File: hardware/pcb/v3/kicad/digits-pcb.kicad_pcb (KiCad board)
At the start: 2 copper layers, 61.9 x 76.2 mm, 77 parts, among them J8 Conn_01x04, SW1 Hook_DPDT, SW2 SW_Push, U10 XL6019E1, U2 DRV8871DDAR, U3 RP2040, U4 W25Q16JVSSIQ, U5 AMS1117-3.3, U6 TLV320AIC3104IRHBR, U7 XC6206P182MR, Y1 ABM8-272-T3

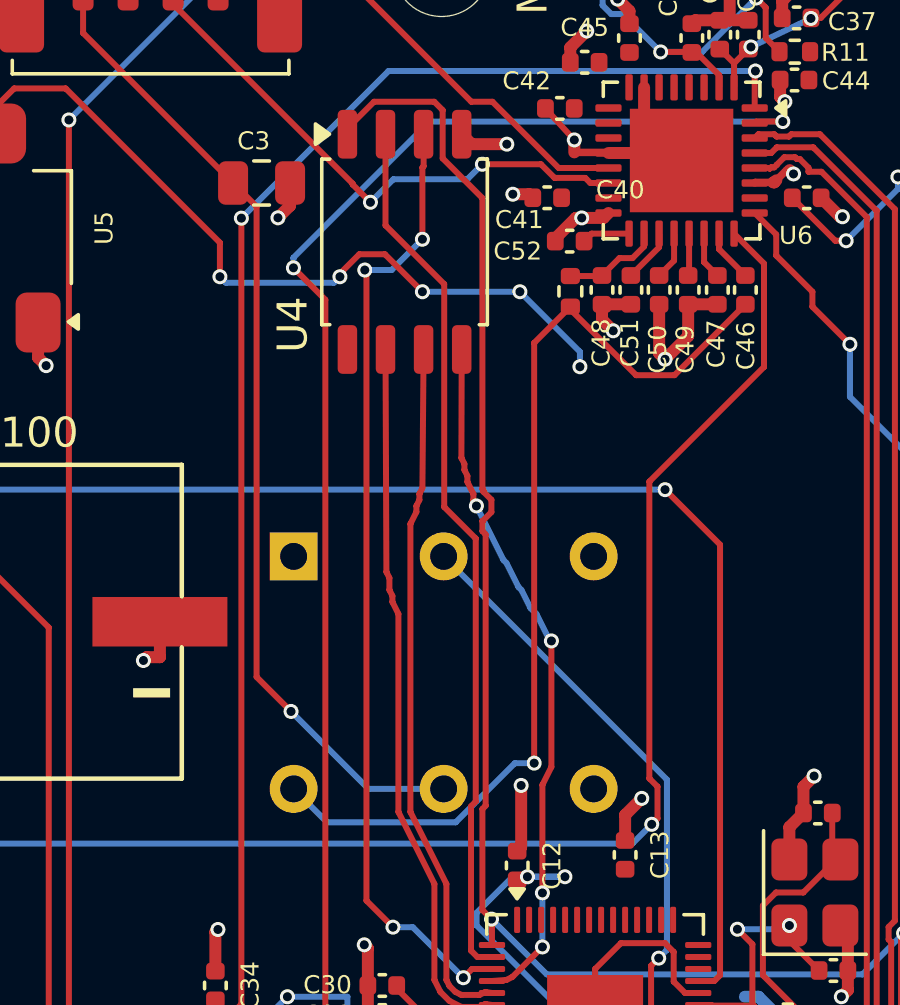
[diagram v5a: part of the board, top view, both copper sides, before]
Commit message: fix(hardware): route SW1 corrected DPDT pin mapping on the PCB
Update-PCB-from-Schematic for the SW1 re-pin (e2b5f92, 6b79142): HOOK_SW,
MIC_FROM_SW, and MIC_HOT moved to pads 3, 4, 6 and rerouted; pad 2 GND
unchanged. BOM regenerated via the JLCPCB toolkit (SW2 now carries C87036,
connector refs annotated). DRC clean: 0 errors, 0 unconnected, 0 parity.
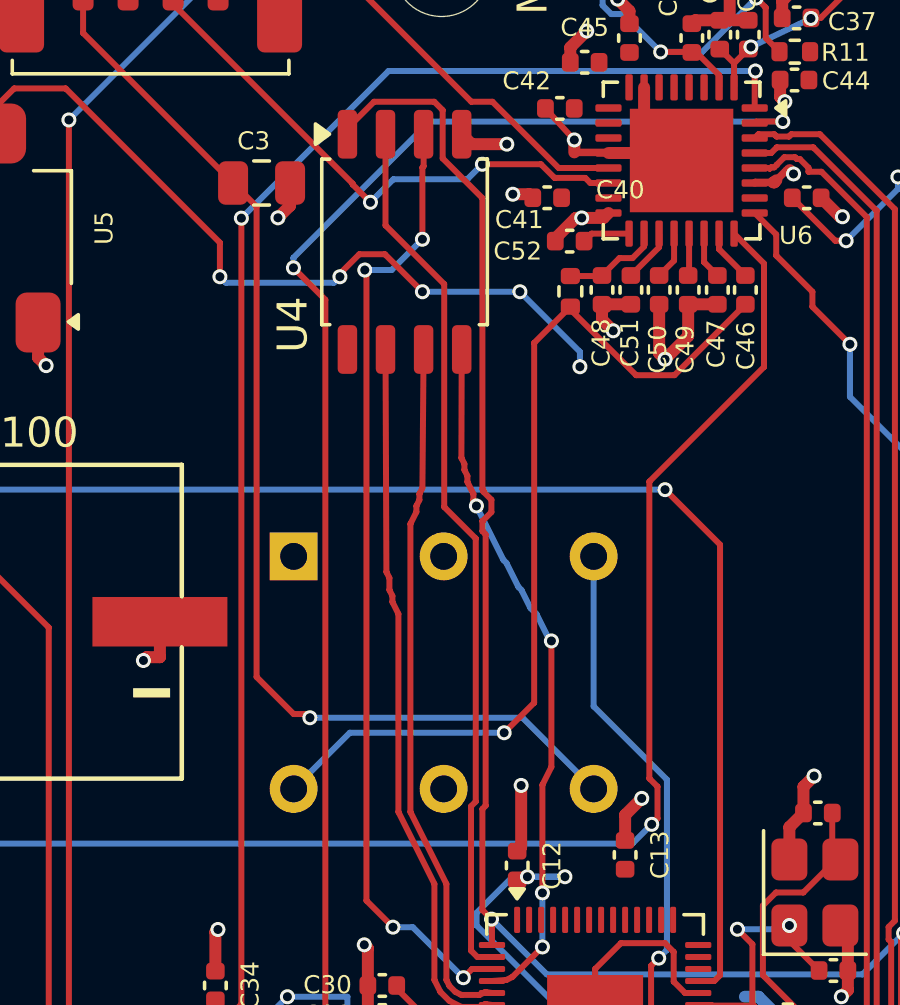
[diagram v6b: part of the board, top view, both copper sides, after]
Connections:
- SW1 pad 2: HOOK_SW -> GND
- SW1 pad 3: GND -> HOOK_SW
- SW1 pad 5: MIC_HOT -> unconnected-(SW1B-B-Pad5)
- SW1 pad 6: unconnected-(SW1B-C-Pad6) -> MIC_HOT
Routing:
- net MIC_HOT: track 34.2 -> 39.2 mm
- net MIC_FROM_SW: track 32.8 -> 30.7 mm
- net HOOK_SW: track 22.3 -> 20.2 mm
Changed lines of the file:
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@@
 			(layers "*.Cu" "*.Mask")
 			(remove_unused_layers no)
-			(net "HOOK_SW")
+			(net "GND")
 			(pinfunction "B_2")
 			(pintype "passive")
@@
 			(layers "*.Cu" "*.Mask")
 			(remove_unused_layers no)
-			(net "GND")
+			(net "HOOK_SW")
 			(pinfunction "C_3")
 			(pintype "passive")
@@
 			(layers "*.Cu" "*.Mask")
 			(remove_unused_layers no)
-			(net "MIC_HOT")
+			(net "unconnected-(SW1B-B-Pad5)")
 			(pinfunction "B_5")
 			(pintype "passive")
@@
 			(layers "*.Cu" "*.Mask")
 			(remove_unused_layers no)
-			(net "unconnected-(SW1B-C-Pad6)")
+			(net "MIC_HOT")
 			(pinfunction "C_6")
-			(pintype "passive+no_connect")
+			(pintype "passive")
 		)
 		(embedded_fonts no)
@@
 	)
 	(segment
-		(start 61.4026 29.242)
-		(end 63.7655 26.8791)
+		(start 56.7253 28.1639)
+		(end 56.7253 40.1597)
 		(width 0.2)
 		(layer "F.Cu")
@@
 	)
 	(segment
-		(start 56.7253 28.1639)
-		(end 56.7253 42.1737)
+		(start 61.4026 29.242)
+		(end 63.7655 26.8791)
 		(width 0.2)
 		(layer "F.Cu")
@@
 	(segment
 		(start 57.932 26.9572)
-		(end 57.932 27.0508)
+		(end 56.7253 28.1639)
 		(width 0.2)
 		(layer "F.Cu")
@@
 	)
 	(segment
-		(start 57.932 27.0508)
-		(end 60.1232 29.242)
+		(start 56.7253 40.1597)
+		(end 55.725 41.16)
 		(width 0.2)
 		(layer "F.Cu")
@@
 	(segment
 		(start 57.932 26.9572)
-		(end 56.7253 28.1639)
+		(end 57.932 27.0508)
+		(width 0.2)
+		(layer "F.Cu")
+		(net "MIC_FROM_SW")
+	)
+	(segment
+		(start 57.932 27.0508)
+		(end 60.1232 29.242)
 		(width 0.2)
 		(layer "F.Cu")
@@
 	)
 	(via
-		(at 56.7253 42.1737)
+		(at 55.725 41.16)
 		(size 0.5)
 		(drill 0.3)
@@
 	)
 	(segment
-		(start 54.1113 44.1454)
-		(end 49.822 44.1454)
-		(width 0.2)
-		(layer "B.Cu")
-		(net "MIC_FROM_SW")
-	)
-	(segment
-		(start 49.822 44.1454)
+		(start 50.5792 41.16)
 		(end 48.7079 43.0313)
 		(width 0.2)
@@
 	)
 	(segment
-		(start 56.083 42.1737)
-		(end 54.1113 44.1454)
-		(width 0.2)
-		(layer "B.Cu")
-		(net "MIC_FROM_SW")
-	)
-	(segment
-		(start 56.7253 42.1737)
-		(end 56.083 42.1737)
+		(start 55.725 41.16)
+		(end 50.5792 41.16)
 		(width 0.2)
 		(layer "B.Cu")
@@
 	(segment
 		(start 61.1502 42.7236)
-		(end 53.7079 35.2813)
+		(end 58.7079 40.2813)
+		(width 0.2)
+		(layer "B.Cu")
+		(net "HOOK_SW")
+	)
+	(segment
+		(start 58.7079 40.2813)
+		(end 58.7079 35.2813)
 		(width 0.2)
 		(layer "B.Cu")
@@
 	)
 	(segment
-		(start 47.4722 39.3015)
-		(end 47.4722 23.6187)
+		(start 49.1272 40.5372)
+		(end 49.25 40.66)
 		(width 0.2)
 		(layer "F.Cu")
@@
 	)
 	(segment
-		(start 47.4722 23.6187)
-		(end 46.689 22.8355)
+		(start 48.7079 40.5372)
+		(end 49.1272 40.5372)
+		(width 0.2)
+		(layer "F.Cu")
+		(net "MIC_HOT")
+	)
+	(segment
+		(start 47.4722 39.3015)
+		(end 48.7079 40.5372)
 		(width 0.2)
 		(layer "F.Cu")
@@
 	)
 	(segment
-		(start 48.621 40.4503)
+		(start 47.4722 23.6187)
 		(end 47.4722 39.3015)
 		(width 0.2)
@@
 		(net "MIC_HOT")
 	)
+	(segment
+		(start 46.689 22.8355)
+		(end 47.4722 23.6187)
+		(width 0.2)
+		(layer "F.Cu")
+		(net "MIC_HOT")
+	)
 	(via
-		(at 48.621 40.4503)
+		(at 49.25 40.66)
 		(size 0.5)
 		(drill 0.3)
@@
 	)
 	(segment
-		(start 48.621 40.4503)
-		(end 51.202 43.0313)
+		(start 56.3366 40.66)
+		(end 58.7079 43.0313)
 		(width 0.2)
 		(layer "B.Cu")
@@
 	)
 	(segment
-		(start 51.202 43.0313)
-		(end 53.7079 43.0313)
+		(start 49.25 40.66)
+		(end 56.3366 40.66)
 		(width 0.2)
 		(layer "B.Cu")

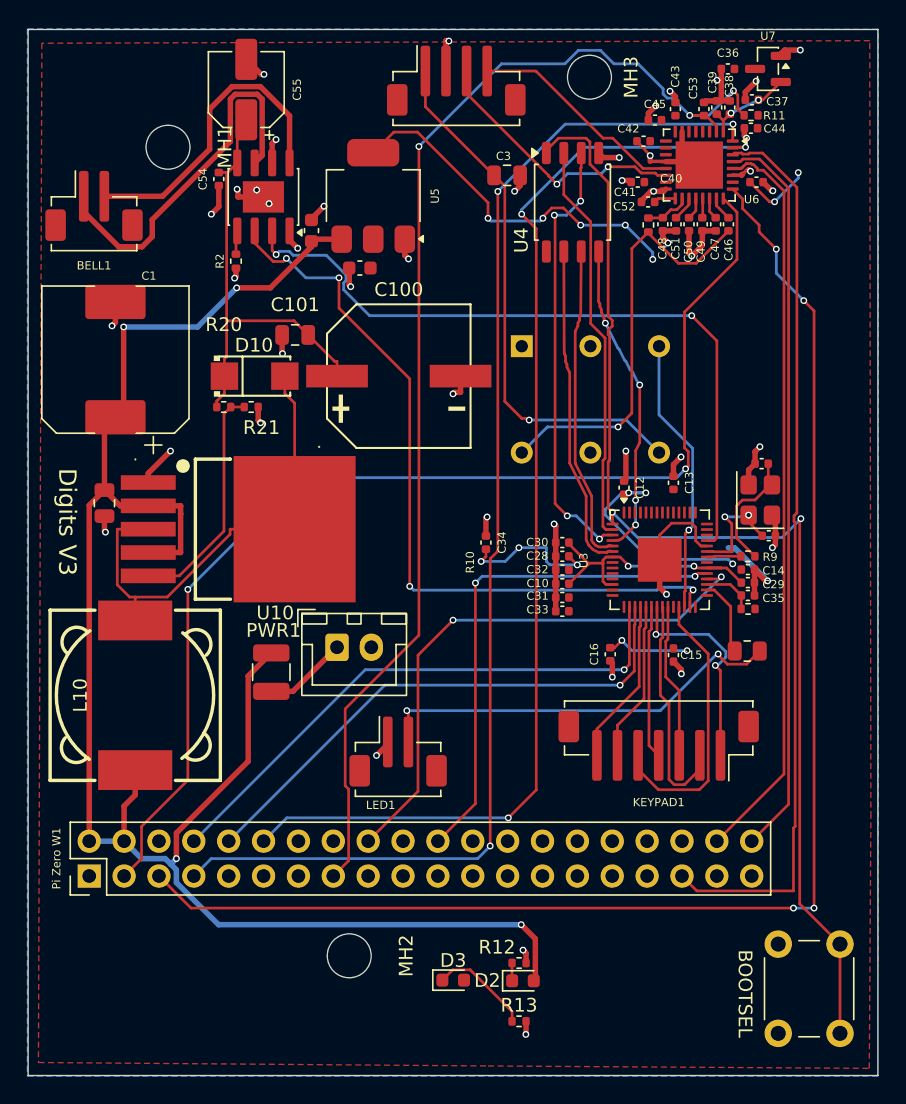
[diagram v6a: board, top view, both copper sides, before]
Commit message: fix(hardware): correct SW1 hook-switch footprint to the IL 2240 5mm pin grid
The SW_DPDT_Hook footprint mis-derived its geometry: the datasheet's
7.45/7.75mm dimensions are mounting-feature offsets, not signal-pin
spacing, so the two pin rows were placed 7.75mm apart instead of the
real 5.0mm. The body outline was also rotated 90 degrees and undersized.

Set the signal pins to the correct 5.0 x 5.0mm grid, redrew the body
outline to 24.4 x 17.2mm (consistent silk/fab/courtyard) with a pin-1
marker, and rerouted the SW1 nets displaced by the pad move. Library
footprint and board instance both updated; DRC clean (0 errors).
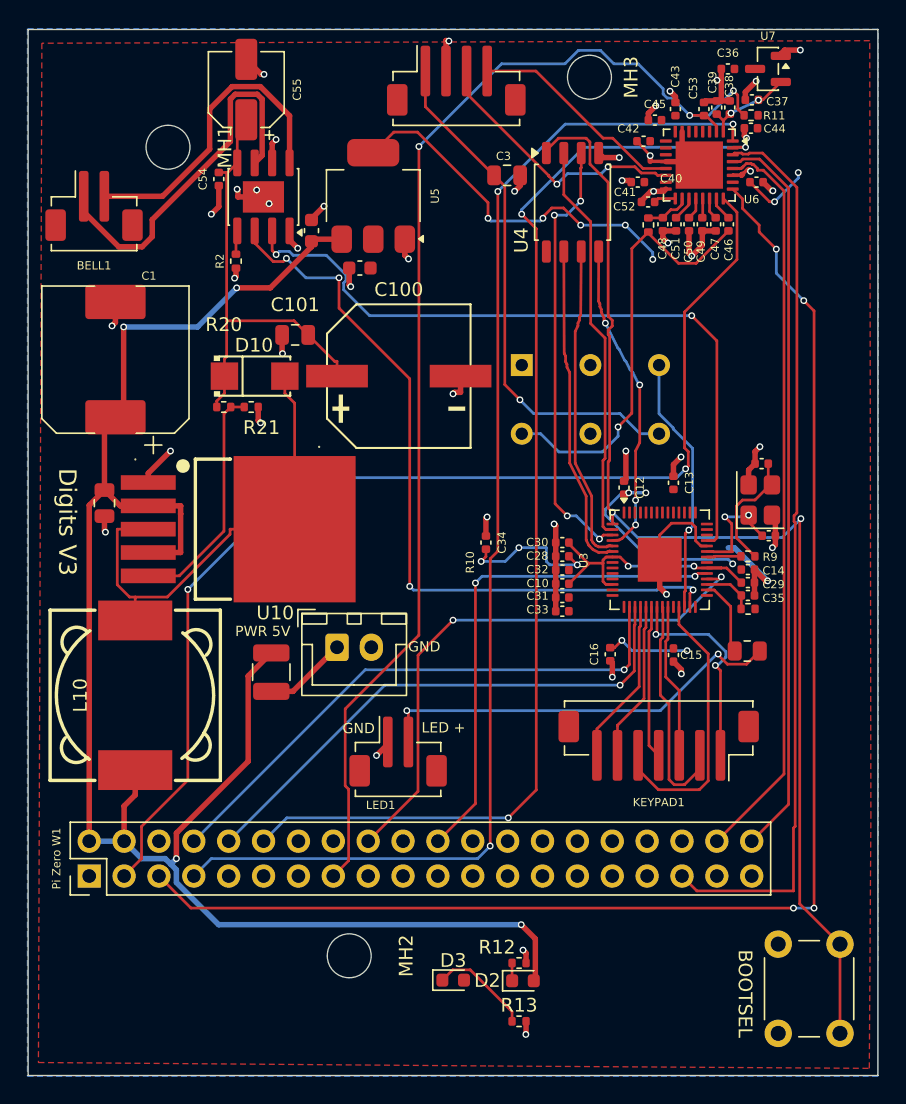
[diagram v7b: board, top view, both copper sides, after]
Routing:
- net HOOK_SW: track 20.2 -> 18.9 mm
- net MIC_HOT: track 39.2 -> 38.0 mm
- net MIC_FROM_SW: track 30.7 -> 31.6 mm
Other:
- board text added: "GND"
- board text added: "LED +"
- board text added: "PWR 5V"
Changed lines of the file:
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@@
 			(at -4.625 -1.225 0)
 			(layer "F.SilkS")
+			(hide yes)
 			(effects
 				(font
@@
 		(layer "B.Cu")
 		(at 53.7079 39.1563 -90)
-		(descr "DPDT telephone hook switch (INH-2240 / IL 2240 family), 6 signal pins, 5.0mm pitch, 7.75mm row spacing, Ø0.9mm signal. Mounting pins not present on common clones - held by signal pins + phone body pressure.")
+		(descr "DPDT telephone hook switch (INH-2240 / IL 2240 family), 6 signal pins, 6 signal pins on a 5.0 x 5.0mm grid, Ø0.9mm. Genuine part has 2x 2.1mm mounting holes, deliberately omitted to match the donor PCB; long signal pins seat the switch. Body 24.4 x 17.2mm.")
 		(tags "switch DPDT hook telephone THT INH-2240 IL-2240")
 		(property "Reference" "SW1"
@@
 		(duplicate_pad_numbers_are_jumpers no)
 		(fp_rect
-			(start -8.85 7.55)
-			(end 8.85 -7.55)
+			(start -8.72 12.32)
+			(end 8.72 -12.32)
 			(stroke
 				(width 0.12)
@@
 		)
 		(fp_rect
-			(start -9.1 11)
-			(end 9.1 -11)
+			(start -8.85 12.45)
+			(end 8.85 -12.45)
 			(stroke
 				(width 0.05)
@@
 		)
 		(fp_rect
-			(start -8.6 7.3)
-			(end 8.6 -7.3)
+			(start -8.6 12.2)
+			(end 8.6 -12.2)
 			(stroke
 				(width 0.1)
@@
 		)
 		(pad "1" thru_hole rect
-			(at -3.875 5 270)
+			(at -2.5 5 270)
 			(size 1.6 1.6)
 			(drill 0.9)
@@
 		)
 		(pad "2" thru_hole circle
-			(at -3.875 0 270)
+			(at -2.5 0 270)
 			(size 1.6 1.6)
 			(drill 0.9)
@@
 		)
 		(pad "3" thru_hole circle
-			(at -3.875 -5 270)
+			(at -2.5 -5 270)
 			(size 1.6 1.6)
 			(drill 0.9)
@@
 		)
 		(pad "4" thru_hole circle
-			(at 3.875 5 270)
+			(at 2.5 5 270)
 			(size 1.6 1.6)
 			(drill 0.9)
@@
 		)
 		(pad "5" thru_hole circle
-			(at 3.875 0 270)
+			(at 2.5 0 270)
 			(size 1.6 1.6)
 			(drill 0.9)
@@
 		)
 		(pad "6" thru_hole circle
-			(at 3.875 -5 270)
+			(at 2.5 -5 270)
 			(size 1.6 1.6)
 			(drill 0.9)
@@
 		(layer "Edge.Cuts")
 	)
+	(gr_text "PWR 5V"
+		(at 27.825 56.485 0)
+		(layer "F.SilkS")
+		(effects
+			(font
+				(size 0.75 0.75)
+			)
+			(justify left bottom)
+		)
+	)
+	(gr_text "GND"
+		(at 35.65 63.56 0)
+		(layer "F.SilkS")
+		(effects
+			(font
+				(size 0.75 0.75)
+			)
+			(justify left bottom)
+		)
+	)
+	(gr_text "GND"
+		(at 40.425 57.61 0)
+		(layer "F.SilkS")
+		(effects
+			(font
+				(size 0.75 0.75)
+			)
+			(justify left bottom)
+		)
+	)
+	(gr_text "LED +"
+		(at 41.4 63.51 0)
+		(layer "F.SilkS")
+		(effects
+			(font
+				(size 0.75 0.75)
+				(thickness 0.09375)
+			)
+			(justify left bottom)
+		)
+	)
 	(gr_text "BOOTSEL"
 		(at 64.388989 79.235 270)
@@
 	)
 	(segment
-		(start 50.5792 41.16)
-		(end 48.7079 43.0313)
+		(start 55.725 41.835)
+		(end 54.575 42.985)
+		(width 0.2)
+		(layer "B.Cu")
+		(net "MIC_FROM_SW")
+	)
+	(segment
+		(start 50.0829 41.6563)
+		(end 48.7079 41.6563)
+		(width 0.2)
+		(layer "B.Cu")
+		(net "MIC_FROM_SW")
+	)
+	(segment
+		(start 54.575 42.985)
+		(end 51.4116 42.985)
+		(width 0.2)
+		(layer "B.Cu")
+		(net "MIC_FROM_SW")
+	)
+	(segment
+		(start 51.4116 42.985)
+		(end 50.0829 41.6563)
 		(width 0.2)
 		(layer "B.Cu")
@@
 	(segment
 		(start 55.725 41.16)
-		(end 50.5792 41.16)
+		(end 55.725 41.835)
 		(width 0.2)
 		(layer "B.Cu")
@@
 	)
 	(segment
-		(start 60.876 48.6736)
-		(end 61.1502 48.3994)
+		(start 59.7379 41.22966)
+		(end 59.7379 41.3113)
 		(width 0.2)
 		(layer "B.Cu")
@@
 	)
 	(segment
-		(start 61.1502 42.7236)
-		(end 58.7079 40.2813)
+		(start 61.1502 48.3994)
+		(end 60.876 48.6736)
 		(width 0.2)
 		(layer "B.Cu")
@@
 	)
 	(segment
-		(start 58.7079 40.2813)
-		(end 58.7079 35.2813)
+		(start 58.7079 40.19966)
+		(end 59.7379 41.22966)
 		(width 0.2)
 		(layer "B.Cu")
@@
 	)
 	(segment
-		(start 61.1502 48.3994)
+		(start 58.7079 36.6563)
+		(end 58.7079 40.19966)
+		(width 0.2)
+		(layer "B.Cu")
+		(net "HOOK_SW")
+	)
+	(segment
+		(start 61.1502 42.7236)
+		(end 61.1502 48.3994)
+		(width 0.2)
+		(layer "B.Cu")
+		(net "HOOK_SW")
+	)
+	(segment
+		(start 59.7379 41.3113)
 		(end 61.1502 42.7236)
 		(width 0.2)
@@
 	)
 	(segment
-		(start 49.1272 40.5372)
-		(end 49.25 40.66)
-		(width 0.2)
-		(layer "F.Cu")
-		(net "MIC_HOT")
-	)
-	(segment
 		(start 41.689 15.2355)
 		(end 41.689 17.8355)
@@
 	)
 	(segment
-		(start 48.7079 40.5372)
-		(end 49.1272 40.5372)
+		(start 48.575 39.185)
+		(end 47.4722 38.0822)
 		(width 0.2)
 		(layer "F.Cu")
@@
 	)
 	(segment
-		(start 47.4722 39.3015)
-		(end 48.7079 40.5372)
+		(start 47.4722 38.0822)
+		(end 47.4722 23.6187)
 		(width 0.2)
 		(layer "F.Cu")
@@
 	(segment
 		(start 47.4722 23.6187)
-		(end 47.4722 39.3015)
-		(width 0.2)
-		(layer "F.Cu")
-		(net "MIC_HOT")
-	)
-	(segment
-		(start 46.689 22.8355)
-		(end 47.4722 23.6187)
+		(end 46.689 22.8355)
 		(width 0.2)
 		(layer "F.Cu")
@@
 	)
 	(via
-		(at 49.25 40.66)
+		(at 48.575 39.185)
 		(size 0.5)
 		(drill 0.3)
@@
 	)
 	(segment
-		(start 56.3366 40.66)
-		(end 58.7079 43.0313)
+		(start 48.575 39.185)
+		(end 49.575 40.185)
+		(width 0.2)
+		(layer "B.Cu")
+		(net "MIC_HOT")
+	)
+	(segment
+		(start 57.3329 41.6563)
+		(end 58.7079 41.6563)
+		(width 0.2)
+		(layer "B.Cu")
+		(net "MIC_HOT")
+	)
+	(segment
+		(start 55.8616 40.185)
+		(end 57.3329 41.6563)
 		(width 0.2)
 		(layer "B.Cu")
@@
 	)
 	(segment
-		(start 49.25 40.66)
-		(end 56.3366 40.66)
+		(start 49.575 40.185)
+		(end 55.8616 40.185)
 		(width 0.2)
 		(layer "B.Cu")

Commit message: fix(hardware): mirror Pi Zero header to the correct mating handedness
V3 placed the Pi Zero 2 W header with the stock KiCad PinHeader_2x20
footprint, which is the mirror image of the deliberately-mirrored
variant the working V2 board uses. The Pi mates face-to-face (its GPIO
pins face up, the carrier comes down onto them), so the carrier
footprint must be the mirror of the Pi pinout for pin 1 to meet pin 1.
The stock footprint would have landed every GPIO on the wrong pin.

Reflected the footprint's pads about its local X axis (no layer flip, so
it stays on F.Cu), matching V2's handedness (pad 3 local Y now -2.54,
winding -6.5 == V2), rerouted all 40 Pi nets, and cleaned the resulting
shorts and clearance violations. DRC clean: 0 errors, 0 unconnected,
0 schematic-parity.
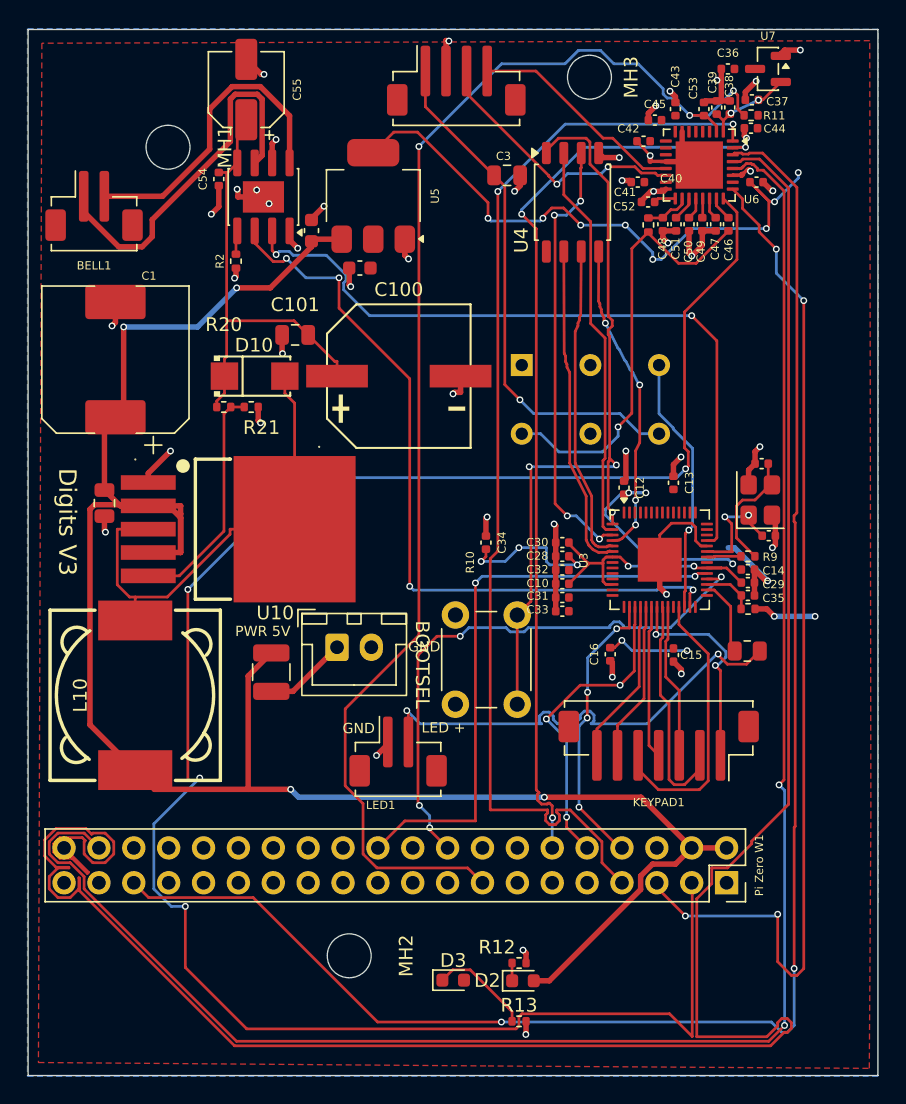
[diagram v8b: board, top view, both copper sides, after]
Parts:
- moved Pi Zero W1 46.4 mm to (63.6, 74.4)
- moved SW2 33.6 mm to (48.4, 61.4)
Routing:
- net CODEC_DIN: track 53.7 -> 165.2 mm
- net CODEC_DOUT: track 54.2 -> 131.4 mm, vias 0 -> 2
- net CODEC_SDA: track 84.6 -> 144.9 mm, vias 2 -> 4
- net CODEC_WCLK: track 65.8 -> 119.9 mm, vias 0 -> 2
- net QSPI_SS: track 86.5 -> 57.6 mm, vias 2 -> 3
- net CODEC_SCL: track 103.5 -> 75.0 mm
- net UART_TX_PI: track 41.3 -> 21.0 mm, vias 1 -> 4
- net +3V3: track 64.7 -> 82.5 mm, vias 15 -> 18
- net UART_RX_PI: track 39.4 -> 23.2 mm, vias 1 -> 3
- net CODEC_BCLK: track 83.3 -> 67.1 mm
- net +5V: track 132.1 -> 145.2 mm
- net CODEC_MCLK: track 90.8 -> 80.6 mm, vias 3 -> 2
- net CODEC_RESET: track 89.5 -> 97.4 mm
- net SWD_SWCLK: track 37.1 -> 42.4 mm
- net LED_A: track 30.5 -> 34.2 mm
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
